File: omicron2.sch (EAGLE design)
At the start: 180 parts, among them IC1 XC6SLX4-2TQG144, IC2 TPS73033DBV, IC3 LD6806TD/12H, IC4 MT48LC64M4A2, IC5 M25P40-2253716, IC6 TPS73033DBV, X1 USB-MICRO-B-BOTTOM, X2 7C-33.3-1842039

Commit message: backup
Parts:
- removed C31, C32: (no value), rcl:C-EUC0603
- TP13, TP14, TP15, TP16: value TPTP15R -> TPTP20R; device testpad:TPTP15R -> testpad:TPTP20R
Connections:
- net CLK_33: now also IC1.IO_L34P_GCLK19_0; no longer IC1.IO_L31P_GCLK31_D14_2
- net GND: no longer C31.2, C32.2
- net LED1: now also IC1.IO_L48P_D7_2
- net LED2: now also IC1.IO_L48N_RDWR_B_VREF_2
- net LED3: now also IC1.IO_L49P_D3_2
- net M_A4: now also IC1.IO_L35P_GCLK17_0; no longer IC1.IO_L32N_1
- net M_PWREN: now also IC1.IO_L32N_1
- net USB_D+: now also IC1.IO_L13N_D10_2; no longer C32.1, IC1.IO_L12N_D2_MISO3_2
- net USB_D-: no longer C31.1
- net USB_PUP: now also IC1.IO_L2P_CMPCLK_2; no longer IC1.IO_L13N_D10_2

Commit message: backup
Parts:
- added C31, C32: 470nF, rcl:C-EUC0603
- added Q1, Q3: (no value), transistors:NPN-BIAS-SOT323-BEC
- added Q2, Q4: BC807W, transistor-pnp:BC807W
- added R60, R61: 6k8 1%, rcl:R-EU_R0603
- TP2: value TPTP15R -> TPTP20R; device testpad:TPTP15R -> testpad:TPTP20R
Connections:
- new net N$24: Q1.C, R60.2
- new net N$25: Q4.B, R61.1
- new net N$26: Q3.C, R61.2
- new net N$7: Q2.B, R60.1
- new net VIO33: IC1.IO_L62P_D5_2, Q3.B
- new net VIO50: IC1.IO_L49N_D4_2, Q1.B
- net +3V3: now also C31.1, C32.1, Q4.E
- net +5V: now also Q2.E
- net GND: now also C31.2, C32.2, Q1.E, Q3.E
- net S10: now also IC1.IO_L41N_GCLK26_3; no longer IC1.IO_L41P_GCLK27_3
- net S11: now also IC1.IO_L37N_3; no longer IC1.IO_L37P_3
- net S12: now also IC1.IO_L36N_3; no longer IC1.IO_L36P_3
- net S13: now also IC1.IO_L2N_3; no longer IC1.IO_L2P_3
- net S14: now also IC1.IO_L1N_VREF_3; no longer IC1.IO_L65P_INIT_B_2
- net S15: now also IC1.IO_L65P_INIT_B_2; no longer IC1.IO_L64P_D8_2
- net S16: now also IC1.IO_L64P_D8_2; no longer IC1.IO_L62P_D5_2
- net S9: now also IC1.IO_L42N_GCLK24_3; no longer IC1.IO_L42P_GCLK25_TRDY2_3
- net SD10: now also IC1.IO_L41P_GCLK27_3; no longer IC1.IO_L37N_3
- net SD11: now also IC1.IO_L37P_3; no longer IC1.IO_L36N_3
- net SD12: now also IC1.IO_L36P_3; no longer IC1.IO_L2N_3
- net SD13: now also IC1.IO_L2P_3; no longer IC1.IO_L1N_VREF_3
- net SD14: now also IC1.IO_L1P_3; no longer IC1.IO_L64N_D9_2
- net SD15: now also IC1.IO_L64N_D9_2; no longer IC1.IO_L62N_D6_2
- net SD16: now also IC1.IO_L62N_D6_2; no longer IC1.IO_L49N_D4_2
- net SD9: now also IC1.IO_L42P_GCLK25_TRDY2_3; no longer IC1.IO_L41N_GCLK26_3
- net VCC_B2: now also Q2.C, Q4.C
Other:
- moved on the sheet: JP10, JP9

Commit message: Initial commit.
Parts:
- added C38, C39: 470nF, rcl:C-EUC0603
- added C40: 2.2uF, rcl:C-EUC0603
- added R62, R63: 68, rcl:R-EU_R0603
- added U$1: PIC10F320, pic10f320:PIC10F320
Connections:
- new net AD_RA0: IC1.IO_L49P_D3_2, U$1.ICSPDAT/RA0
- new net AD_RA1: IC1.IO_L48N_RDWR_B_VREF_2, U$1.ICSPCLK/RA1
- new net AD_RA3: IC1.IO_L31P_GCLK31_D14_2, U$1.MCLRB/VPP/RA3
- new net N$27: C39.1, R62.2, R63.2, U$1.RA2
- net +3V3: now also C38.1, U$1.VCC
- net +5V: now also C40.1
- net GND: now also C38.2, C39.2, C40.2, R62.1, U$1.GND
- net LED1: now also IC1.IO_L3N_0; no longer IC1.IO_L48P_D7_2
- net LED2: now also IC1.IO_L4P_0; no longer IC1.IO_L48N_RDWR_B_VREF_2
- net LED3: now also IC1.IO_L34N_GCLK18_0; no longer IC1.IO_L49P_D3_2
- net VCC_B2: now also R63.1

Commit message: Final touches.
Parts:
- added C41, C42, C43: 470nF, rcl:C-EUC0603
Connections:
- net GND: now also C41.2, C42.2, C43.2
- net VCC_MEM: now also C41.1, C42.1, C43.1
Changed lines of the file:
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@@
 <part name="C40" library="rcl" deviceset="C-EU" device="C0603" value="2.2uF"/>
 <part name="GND106" library="supply1" deviceset="GND" device=""/>
+<part name="C41" library="rcl" deviceset="C-EU" device="C0603" value="470nF"/>
+<part name="C42" library="rcl" deviceset="C-EU" device="C0603" value="470nF"/>
+<part name="C43" library="rcl" deviceset="C-EU" device="C0603" value="470nF"/>
+<part name="GND107" library="supply1" deviceset="GND" device=""/>
+<part name="GND108" library="supply1" deviceset="GND" device=""/>
+<part name="GND109" library="supply1" deviceset="GND" device=""/>
 </parts>
 <sheets>
@@
 <instance part="C40" gate="G$1" x="15.24" y="152.4"/>
 <instance part="GND106" gate="1" x="15.24" y="144.78"/>
+<instance part="C41" gate="G$1" x="88.9" y="53.34"/>
+<instance part="C42" gate="G$1" x="81.28" y="53.34"/>
+<instance part="C43" gate="G$1" x="73.66" y="53.34"/>
+<instance part="GND107" gate="1" x="73.66" y="45.72"/>
+<instance part="GND108" gate="1" x="81.28" y="45.72"/>
+<instance part="GND109" gate="1" x="88.9" y="45.72"/>
 </instances>
 <busses>
@@
 <pinref part="C40" gate="G$1" pin="2"/>
 <pinref part="GND106" gate="1" pin="GND"/>
+</segment>
+<segment>
+<pinref part="C43" gate="G$1" pin="2"/>
+<pinref part="GND107" gate="1" pin="GND"/>
+</segment>
+<segment>
+<pinref part="C42" gate="G$1" pin="2"/>
+<pinref part="GND108" gate="1" pin="GND"/>
+</segment>
+<segment>
+<pinref part="C41" gate="G$1" pin="2"/>
+<pinref part="GND109" gate="1" pin="GND"/>
 </segment>
 </net>
@@
 <pinref part="IC4" gate="P" pin="VDD@2"/>
 <pinref part="IC4" gate="P" pin="VDD@3"/>
-</segment>
-</net>
+<pinref part="C41" gate="G$1" pin="1"/>
+<wire x1="88.9" y1="55.88" x2="88.9" y2="58.42" width="0.1524" layer="91"/>
+<wire x1="88.9" y1="58.42" x2="96.52" y2="58.42" width="0.1524" layer="91"/>
+<pinref part="C42" gate="G$1" pin="1"/>
+<wire x1="81.28" y1="55.88" x2="81.28" y2="58.42" width="0.1524" layer="91"/>
+<wire x1="81.28" y1="58.42" x2="88.9" y2="58.42" width="0.1524" layer="91"/>
+<pinref part="C43" gate="G$1" pin="1"/>
+<wire x1="73.66" y1="55.88" x2="73.66" y2="58.42" width="0.1524" layer="91"/>
+<wire x1="73.66" y1="58.42" x2="81.28" y2="58.42" width="0.1524" layer="91"/>
+</segment>
+</net>

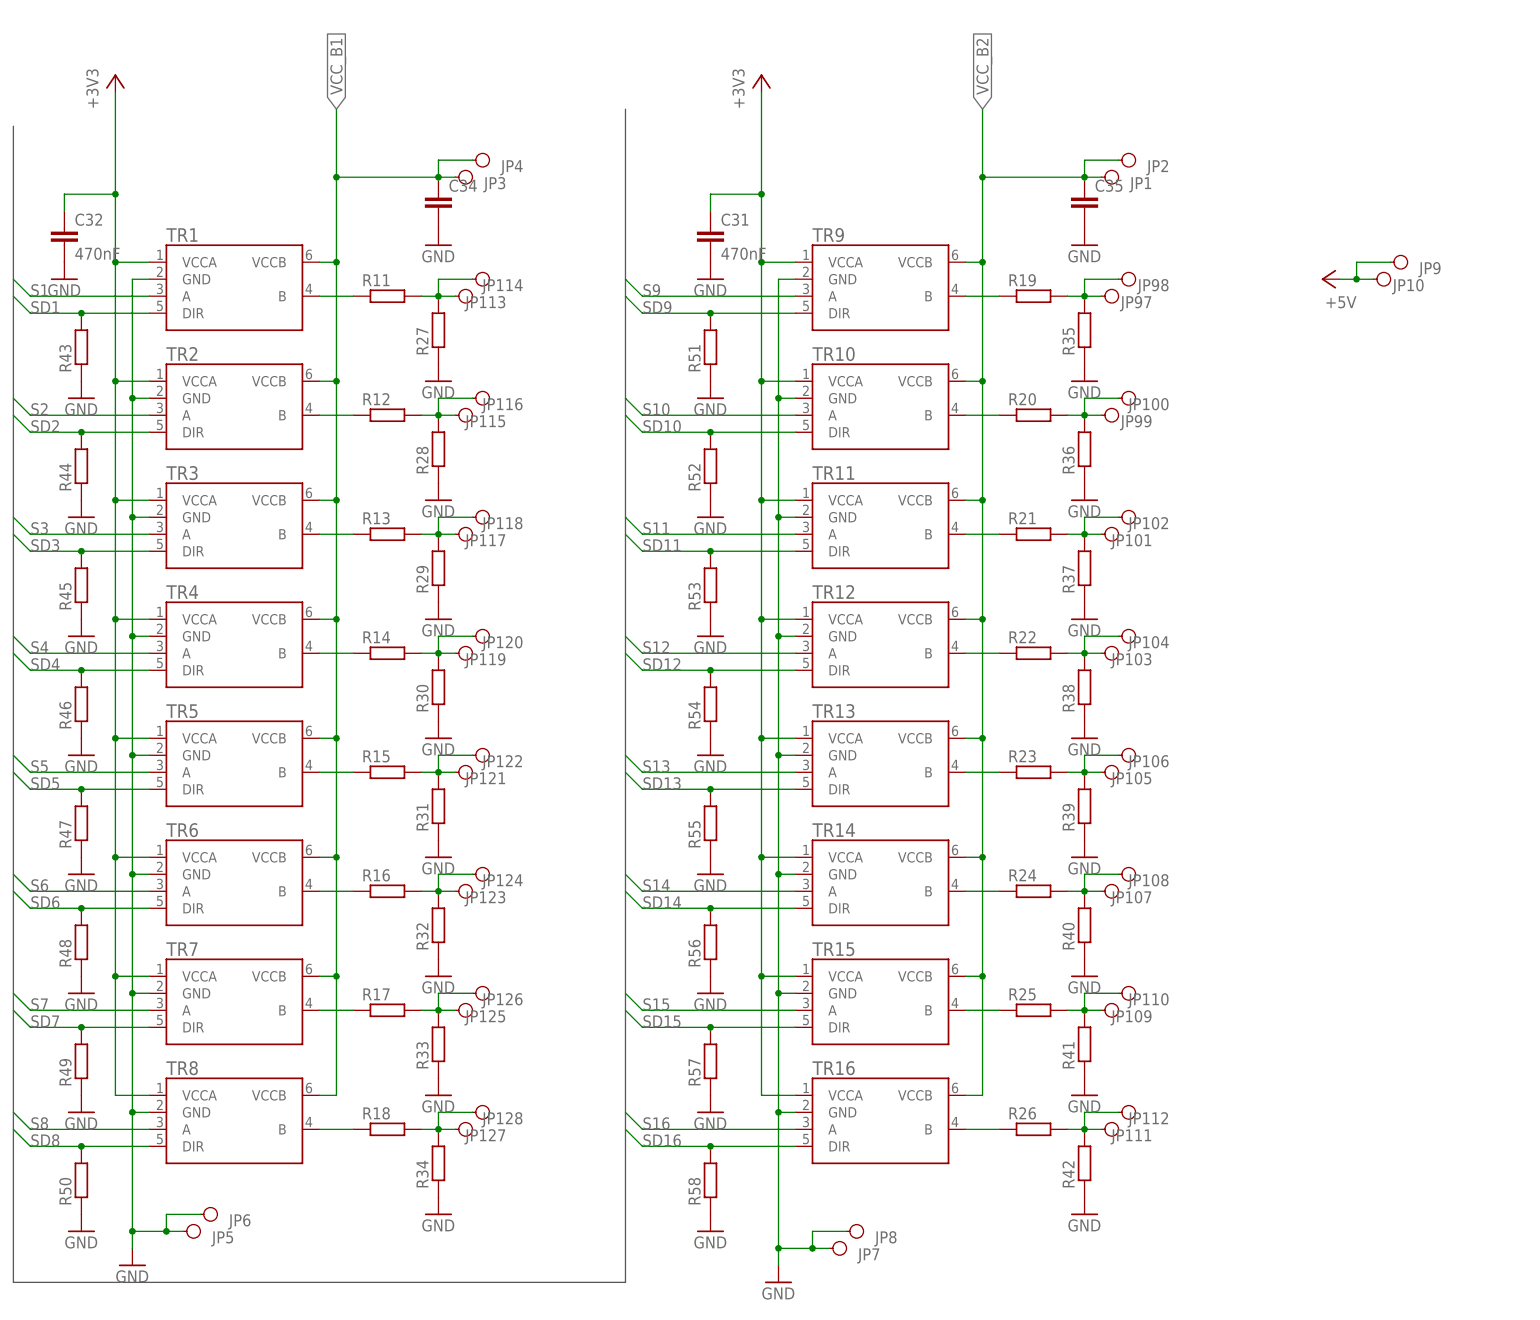
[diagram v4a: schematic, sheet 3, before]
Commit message: v2.0 component values
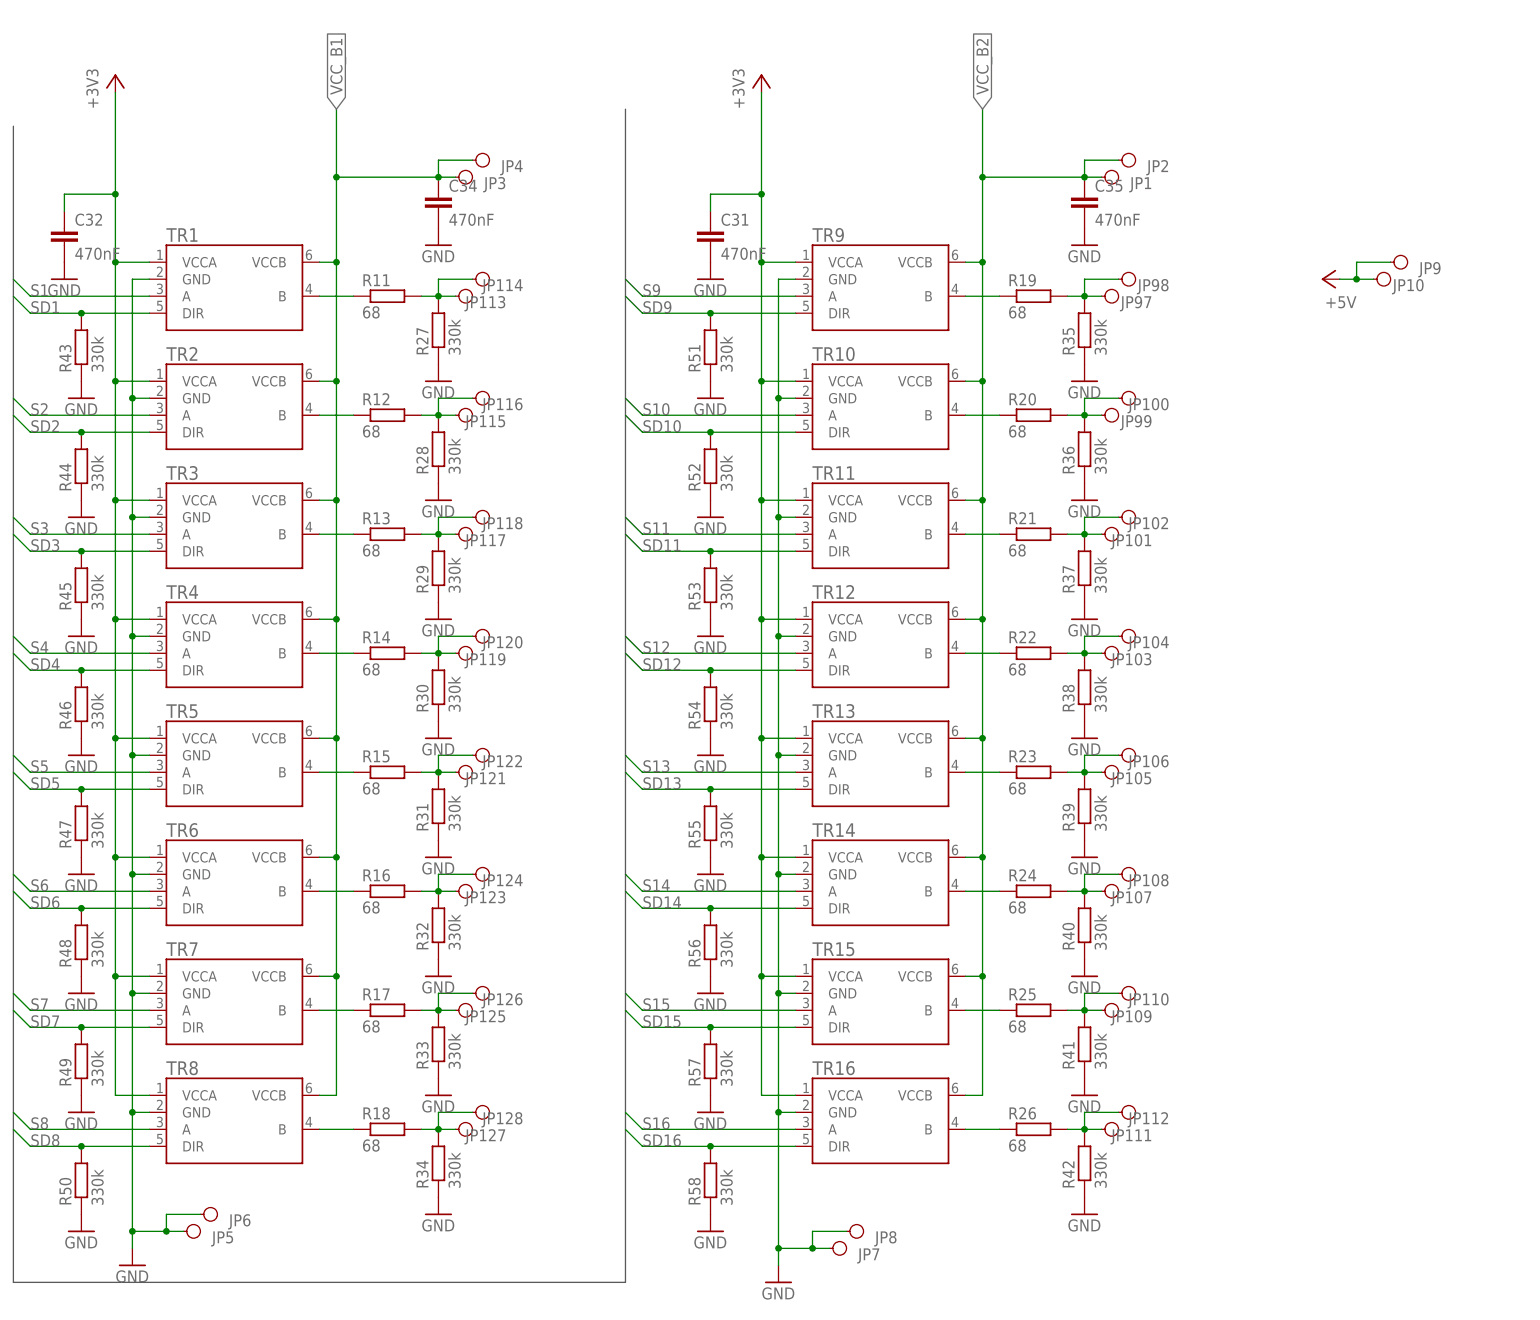
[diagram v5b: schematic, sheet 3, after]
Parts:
- C1, C36: value 10uF -> 10nF
- C34, C35: value (none) -> 470nF
- C39: value 470nF -> 10nF
- C5: value 1uF -> 2.2uF
- IC1: value XC6SLX4-2TQG144 -> XC6SLX4-1876221
- IC2, IC6: value TPS73033DBV -> TPS73033DBV-1135395
- IC3: value LD6806TD/12H -> LD6806TD/12H-2095494
- IC4: value MT48LC64M4A2 -> H57V2562GTR-75C-1907383
- L1, L2, L3: value (none) -> 100nH
- LED5: value RED -> RED-2099221
- Q1, Q3: value (none) -> PDTC123-1757992
- R1, R2: value 27 -> 27 1%
- R11, R12, R13, R14, R15, R16, R17, R18, R19, R20, R21, R22, R23, R24, R25, R26: value (none) -> 68
- R27, R28, R29, R30, R31, R32, R33, R34, R35, R36, R37, R38, R39, R40, R41, R42, R43, R44, R45, R46, R47, R48, R49, R50, R51, R52, R53, R54, R55, R56, R57, R58: value (none) -> 330k
- R5, R7: value 47k -> 330k
- R62: value 68 -> 6k8 1%
- R63: value 68 -> 4k7 1%
- U$1: value PIC10F320 -> PIC10F320-2074912
